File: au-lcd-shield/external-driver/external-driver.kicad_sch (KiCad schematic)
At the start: 6 parts, among them IC2 DSLVDS1047PWR, J1 Power, J2 Backlight, J4 Conn_02x09_Odd_Even, U1 UA78M33CDCYR

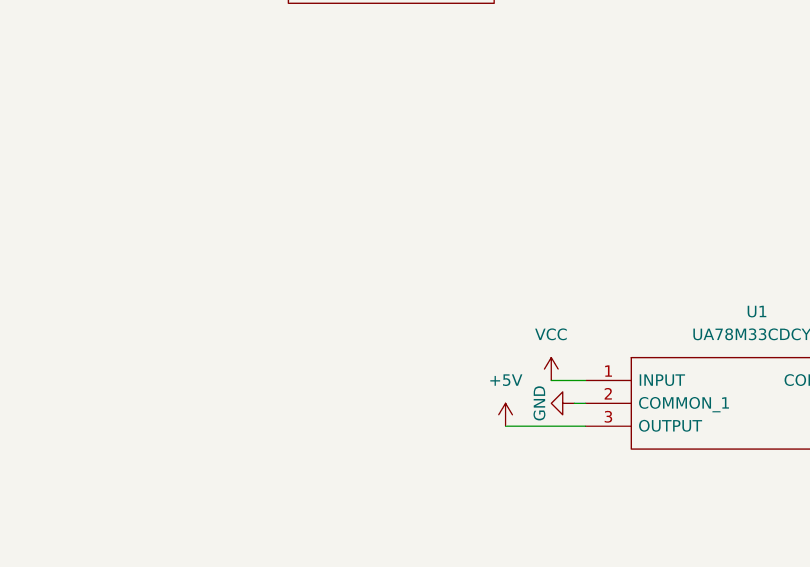
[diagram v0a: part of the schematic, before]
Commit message: add filtering caps for ldo's
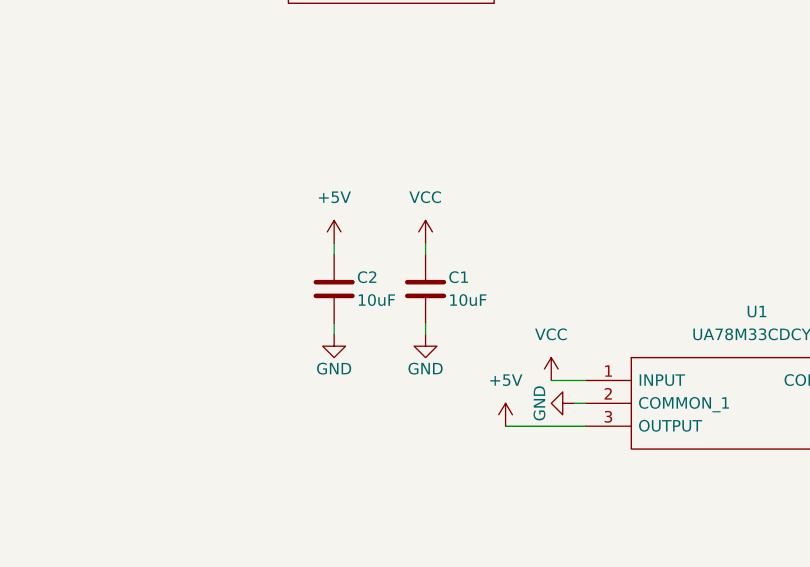
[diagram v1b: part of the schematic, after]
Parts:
- added C1, C2: 10uF, Capacitor_SMD:C_0603_1608Metric_Pad1.08x0.95mm_HandSolder, symbol Device:C
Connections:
- net +5V: now also C2.2
- net GND: now also C1.1, C2.1
- net VCC: now also C1.2
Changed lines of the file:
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@@
+    (stroke (width 0) (type default))
+  )
+  (wire (pts (xy 207.01 140.97) (xy 207.01 139.7))
     (stroke (width 0) (type default))
   )
@@
     (stroke (width 0) (type default))
   )
+  (wire (pts (xy 217.17 149.86) (xy 217.17 148.59))
+    (stroke (width 0) (type default))
+  )
   (wire (pts (xy 50.8 87.63) (xy 50.8 72.39))
     (stroke (width 0) (type default))
@@
     (stroke (width 0) (type default))
   )
+  (wire (pts (xy 217.17 139.7) (xy 217.17 140.97))
+    (stroke (width 0) (type default))
+  )
   (wire (pts (xy 49.53 64.77) (xy 48.26 64.77))
     (stroke (width 0) (type default))
@@
   )
   (wire (pts (xy 27.94 166.37) (xy 29.21 166.37))
+    (stroke (width 0) (type default))
+  )
+  (wire (pts (xy 207.01 149.86) (xy 207.01 148.59))
     (stroke (width 0) (type default))
   )
@@
         (path "/79f54c60-529b-4cec-a4d1-fd8b43a074a1"
           (reference "#PWR013") (unit 1)
+        )
+      )
+    )
+  )
+  (symbol (lib_id "Device:C") (at 217.17 144.78 180) (unit 1)
+    (in_bom yes) (on_board yes) (dnp no)
+    (property "Reference" "C1" (at 219.71 143.51 0)
+      (effects (font (size 1.27 1.27)) (justify right))
+    )
+    (property "Value" "10uF" (at 219.71 146.05 0)
+      (effects (font (size 1.27 1.27)) (justify right))
+    )
+    (property "Footprint" "Capacitor_SMD:C_0603_1608Metric_Pad1.08x0.95mm_HandSolder" (at 216.2048 140.97 0)
+      (effects (font (size 1.27 1.27)) hide)
+    )
+    (property "Datasheet" "~" (at 217.17 144.78 0)
+      (effects (font (size 1.27 1.27)) hide)
+    )
+    (pin "1")
+    (pin "2")
+    (instances
+      (project "external-driver"
+        (path "/79f54c60-529b-4cec-a4d1-fd8b43a074a1"
+          (reference "C1") (unit 1)
         )
       )
@@
     )
   )
+  (symbol (lib_id "power:GND") (at 207.01 149.86 0) (unit 1)
+    (in_bom yes) (on_board yes) (dnp no)
+    (property "Reference" "#PWR01" (at 207.01 156.21 0)
+      (effects (font (size 1.27 1.27)) hide)
+    )
+    (property "Value" "GND" (at 207.01 153.67 0)
+      (effects (font (size 1.27 1.27)))
+    )
+    (property "Footprint" "" (at 207.01 149.86 0)
+      (effects (font (size 1.27 1.27)) hide)
+    )
+    (property "Datasheet" "" (at 207.01 149.86 0)
+      (effects (font (size 1.27 1.27)) hide)
+    )
+    (pin "1")
+    (instances
+      (project "external-driver"
+        (path "/79f54c60-529b-4cec-a4d1-fd8b43a074a1"
+          (reference "#PWR01") (unit 1)
+        )
+      )
+    )
+  )
   (symbol (lib_id "power:+5V") (at 57.15 111.76 0) (mirror y) (unit 1)
     (in_bom yes) (on_board yes) (dnp no)
@@
         (path "/79f54c60-529b-4cec-a4d1-fd8b43a074a1"
           (reference "#PWR02") (unit 1)
+        )
+      )
+    )
+  )
+  (symbol (lib_id "power:+5V") (at 207.01 139.7 0) (mirror y) (unit 1)
+    (in_bom yes) (on_board yes) (dnp no)
+    (property "Reference" "#PWR07" (at 207.01 143.51 0)
+      (effects (font (size 1.27 1.27)) hide)
+    )
+    (property "Value" "+5V" (at 207.01 134.62 0)
+      (effects (font (size 1.27 1.27)))
+    )
+    (property "Footprint" "" (at 207.01 139.7 0)
+      (effects (font (size 1.27 1.27)) hide)
+    )
+    (property "Datasheet" "" (at 207.01 139.7 0)
+      (effects (font (size 1.27 1.27)) hide)
+    )
+    (pin "1")
+    (instances
+      (project "external-driver"
+        (path "/79f54c60-529b-4cec-a4d1-fd8b43a074a1"
+          (reference "#PWR07") (unit 1)
         )
       )
@@
     )
   )
+  (symbol (lib_id "power:GND") (at 217.17 149.86 0) (unit 1)
+    (in_bom yes) (on_board yes) (dnp no)
+    (property "Reference" "#PWR05" (at 217.17 156.21 0)
+      (effects (font (size 1.27 1.27)) hide)
+    )
+    (property "Value" "GND" (at 217.17 153.67 0)
+      (effects (font (size 1.27 1.27)))
+    )
+    (property "Footprint" "" (at 217.17 149.86 0)
+      (effects (font (size 1.27 1.27)) hide)
+    )
+    (property "Datasheet" "" (at 217.17 149.86 0)
+      (effects (font (size 1.27 1.27)) hide)
+    )
+    (pin "1")
+    (instances
+      (project "external-driver"
+        (path "/79f54c60-529b-4cec-a4d1-fd8b43a074a1"
+          (reference "#PWR05") (unit 1)
+        )
+      )
+    )
+  )
   (symbol (lib_id "power:VCC") (at 256.54 60.96 0) (unit 1)
     (in_bom yes) (on_board yes) (dnp no) (fields_autoplaced)
@@
         (path "/79f54c60-529b-4cec-a4d1-fd8b43a074a1"
           (reference "#PWR029") (unit 1)
+        )
+      )
+    )
+  )
+  (symbol (lib_id "Device:C") (at 207.01 144.78 180) (unit 1)
+    (in_bom yes) (on_board yes) (dnp no)
+    (property "Reference" "C2" (at 209.55 143.51 0)
+      (effects (font (size 1.27 1.27)) (justify right))
+    )
+    (property "Value" "10uF" (at 209.55 146.05 0)
+      (effects (font (size 1.27 1.27)) (justify right))
+    )
+    (property "Footprint" "Capacitor_SMD:C_0603_1608Metric_Pad1.08x0.95mm_HandSolder" (at 206.0448 140.97 0)
+      (effects (font (size 1.27 1.27)) hide)
+    )
+    (property "Datasheet" "~" (at 207.01 144.78 0)
+      (effects (font (size 1.27 1.27)) hide)
+    )
+    (pin "1")
+    (pin "2")
+    (instances
+      (project "external-driver"
+        (path "/79f54c60-529b-4cec-a4d1-fd8b43a074a1"
+          (reference "C2") (unit 1)
         )
       )
@@
         )
       )
+    )
+  )
+  (symbol (lib_id "power:VCC") (at 217.17 139.7 0) (unit 1)
+    (in_bom yes) (on_board yes) (dnp no) (fields_autoplaced)
+    (property "Reference" "#PWR011" (at 217.17 143.51 0)
+      (effects (font (size 1.27 1.27)) hide)
+    )
+    (property "Value" "VCC" (at 217.17 134.62 0)
+      (effects (font (size 1.27 1.27)))
+    )
+    (property "Footprint" "" (at 217.17 139.7 0)
+      (effects (font (size 1.27 1.27)) hide)
+    )
+    (property "Datasheet" "" (at 217.17 139.7 0)
+      (effects (font (size 1.27 1.27)) hide)
+    )
+    (pin "1")
+    (instances
+      (project "external-driver"
+        (path "/79f54c60-529b-4cec-a4d1-fd8b43a074a1"
+          (reference "#PWR011") (unit 1)
+        )
+      )

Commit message: pcb v1.0
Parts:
- removed U1: UA78M33CDCYR, SamacSys_Parts:SOT230P700X180-4N, symbol SamacSys_Parts:UA78M33CDCYR
- added U1: 78M05, Package_TO_SOT_SMD:TO-252-2, symbol Regulator_Linear:IFX27001TFV
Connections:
- net +5V: now also U1.3 (OUT)
- net GND: now also U1.2 (GND)
- net VCC: now also U1.1 (IN)

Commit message: fix pins WIP
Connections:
- net TX1_B_IN: now also B1.B_12 (F4); no longer B1.B_5 (A2)
- net TXCLK_B_IN: now also B1.B_9 (F2); no longer B1.B_2 (D1)
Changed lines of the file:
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@@
+    (stroke (width 0) (type default))
+  )
+  (wire (pts (xy 80.01 46.99) (xy 86.36 46.99))
     (stroke (width 0) (type default))
   )
@@
     (stroke (width 0) (type default))
   )
-  (wire (pts (xy 80.01 36.83) (xy 86.36 36.83))
-    (stroke (width 0) (type default))
-  )
   (wire (pts (xy 257.81 27.94) (xy 261.62 27.94))
     (stroke (width 0) (type default))
@@
     (stroke (width 0) (type default))
   )
+  (wire (pts (xy 80.01 54.61) (xy 86.36 54.61))
+    (stroke (width 0) (type default))
+  )
   (wire (pts (xy 50.8 111.76) (xy 50.8 128.27))
     (stroke (width 0) (type default))
@@
   )
   (wire (pts (xy 48.26 34.29) (xy 49.53 34.29))
-    (stroke (width 0) (type default))
-  )
-  (wire (pts (xy 80.01 29.21) (xy 86.36 29.21))
     (stroke (width 0) (type default))
   )
@@
     )
   )
-  (global_label "TXCLK_B_IN" (shape input) (at 80.01 29.21 180) (fields_autoplaced)
-    (effects (font (size 1.27 1.27)) (justify right))
-    (property "Intersheetrefs" "${INTERSHEET_REFS}" (at 66.1391 29.21 0)
-      (effects (font (size 1.27 1.27)) (justify right) hide)
-    )
-  )
   (global_label "TX0_P" (shape input) (at 233.68 107.95 0) (fields_autoplaced)
     (effects (font (size 1.27 1.27)) (justify left))
@@
     )
   )
-  (global_label "TX1_B_IN" (shape input) (at 80.01 36.83 180) (fields_autoplaced)
+  (global_label "TXCLK_B_IN" (shape input) (at 80.01 46.99 180) (fields_autoplaced)
     (effects (font (size 1.27 1.27)) (justify right))
-    (property "Intersheetrefs" "${INTERSHEET_REFS}" (at 68.4977 36.83 0)
+    (property "Intersheetrefs" "${INTERSHEET_REFS}" (at 66.1391 46.99 0)
       (effects (font (size 1.27 1.27)) (justify right) hide)
     )
@@
     )
   )
+  (global_label "TX1_B_IN" (shape input) (at 80.01 54.61 180) (fields_autoplaced)
+    (effects (font (size 1.27 1.27)) (justify right))
+    (property "Intersheetrefs" "${INTERSHEET_REFS}" (at 68.4977 54.61 0)
+      (effects (font (size 1.27 1.27)) (justify right) hide)
+    )
+  )
   (global_label "TX1_B_IN" (shape input) (at 195.58 105.41 180) (fields_autoplaced)
     (effects (font (size 1.27 1.27)) (justify right))
@@
     )
   )
-  (symbol (lib_id "Alchitry_Element:Alchitry_Element_AU") (at 38.1 140.97 0) (unit 3)
+  (symbol (lib_name "Alchitry_Element_AU_1") (lib_id "Alchitry_Element:Alchitry_Element_AU") (at 38.1 140.97 0) (unit 3)
     (in_bom yes) (on_board yes) (dnp no) (fields_autoplaced)
     (property "Reference" "B1" (at 34.29 109.728 0)
@@
     )
   )
-  (symbol (lib_id "Alchitry_Element:Alchitry_Element_AU") (at 95.25 54.61 0) (unit 2)
+  (symbol (lib_name "Alchitry_Element_AU_3") (lib_id "Alchitry_Element:Alchitry_Element_AU") (at 95.25 54.61 0) (unit 2)
     (in_bom yes) (on_board yes) (dnp no) (fields_autoplaced)
     (property "Reference" "B1" (at 91.44 23.368 0)
@@
     )
   )
-  (symbol (lib_id "Alchitry_Element:Alchitry_Element_AU") (at 95.25 140.97 0) (unit 4)
+  (symbol (lib_name "Alchitry_Element_AU_2") (lib_id "Alchitry_Element:Alchitry_Element_AU") (at 95.25 140.97 0) (unit 4)
     (in_bom yes) (on_board yes) (dnp no) (fields_autoplaced)
     (property "Reference" "B1" (at 91.44 109.728 0)
